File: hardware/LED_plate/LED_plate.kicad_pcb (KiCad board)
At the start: 2 copper layers, 77 x 48.5 mm, 17 parts, among them P3 CONN_01X16

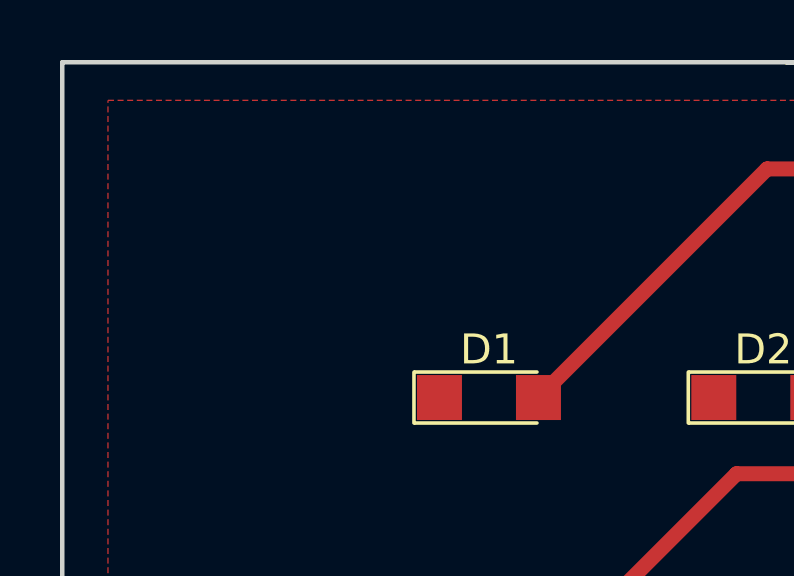
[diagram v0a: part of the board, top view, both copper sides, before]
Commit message: added text to Front layer
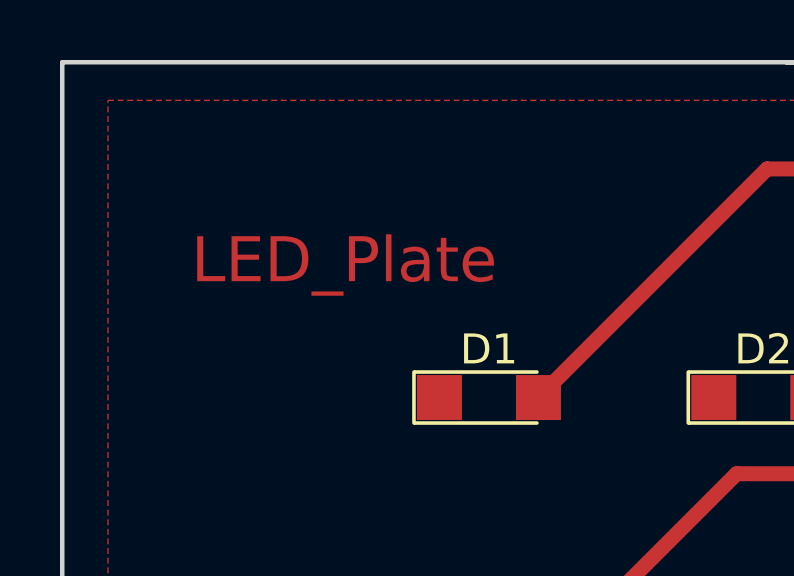
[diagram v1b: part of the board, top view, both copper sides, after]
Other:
- board text added: "LED_Plate"
